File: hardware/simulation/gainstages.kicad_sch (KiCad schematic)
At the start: 21 parts, among them U1 ${SIM.PARAMS}, U2 ${SIM.PARAMS}

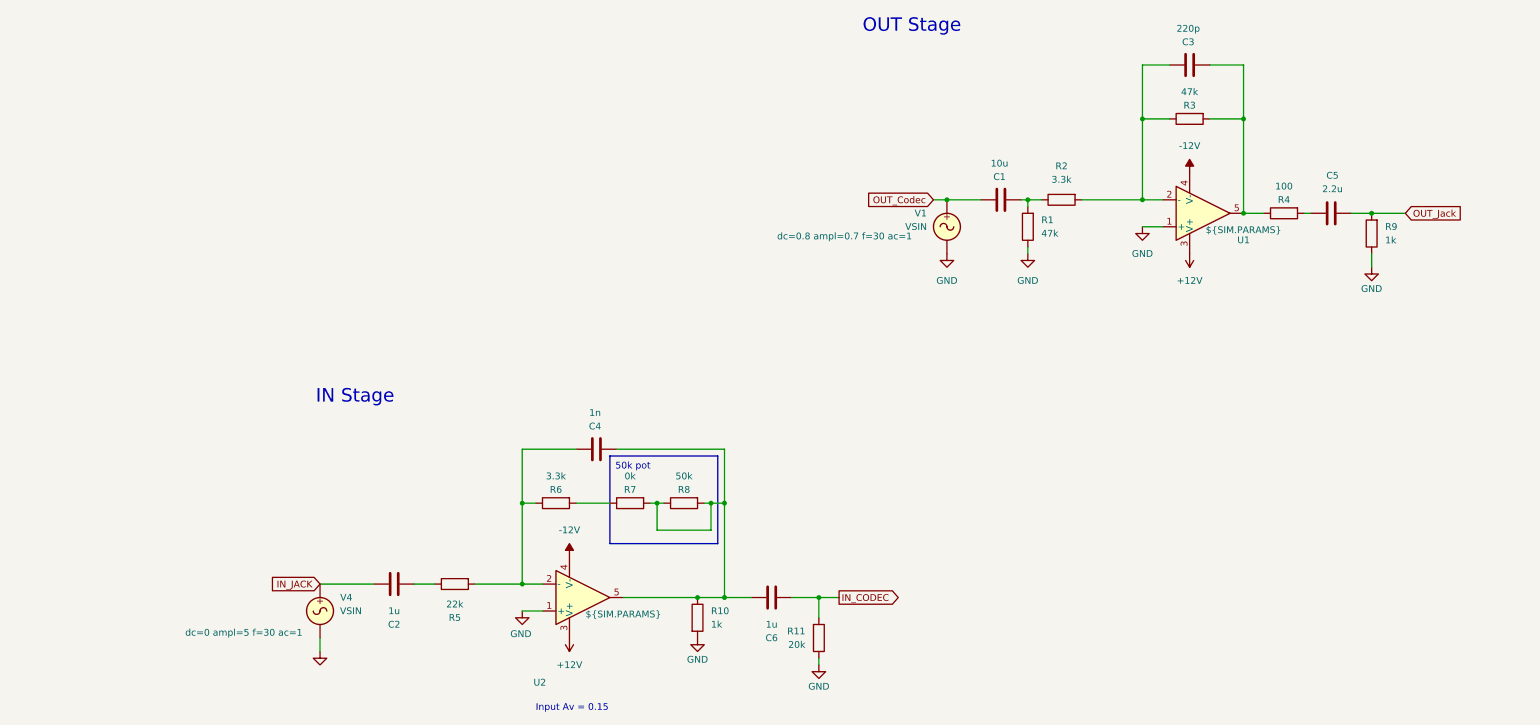
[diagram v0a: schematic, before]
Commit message: update gainstage simulations
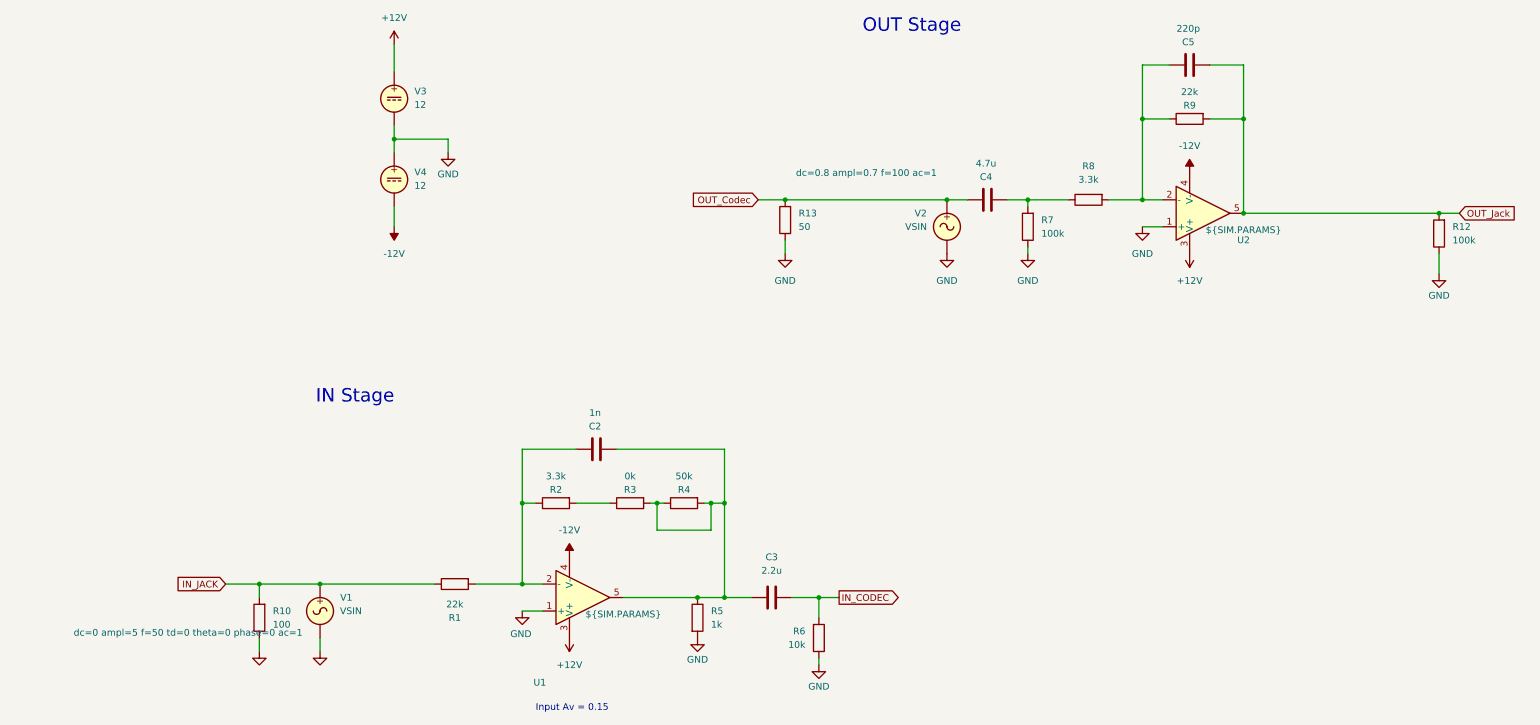
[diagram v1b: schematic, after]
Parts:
- removed C2: 1u, symbol Device:C
- removed C5: 2.2u, symbol Device:C
- removed R4: 100, symbol Device:R
- removed R9: 1k, symbol Device:R
- added R10: 100, symbol Device:R
- added R12: 100k, symbol Device:R
- added R13: 50, symbol Device:R
- added V3, V4: 12, symbol Simulation_SPICE:VDC
- C3: renamed from C6; value 1u -> 2.2u
- C4: renamed from C1; value 10u -> 4.7u
- R6: renamed from R11; value 20k -> 10k
- R7: renamed from R1; value 47k -> 100k
- R9: renamed from R3; value 47k -> 22k
- renumbered C4 to C2, C3 to C5, R5 to R1, R6 to R2, R7 to R3, R8 to R4, R10 to R5, R2 to R8, U2 to U1, U1 to U2, V4 to V1, V1 to V2
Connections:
- net +12V: now also V3.1
- net -12V: now also V4.2
- net GND: now also R10.1, R12.1, R13.1, V3.2, V4.1
- net IN_JACK: now also R1.1, R10.2
- net OUT_Codec: now also R13.2
- net OUT_Jack: now also C5.1, R9.2, U2.5, R12.2
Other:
- moved on the sheet: C4, R8
